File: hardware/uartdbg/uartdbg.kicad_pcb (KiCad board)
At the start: 2 copper layers, 40 x 16.5 mm, 20 parts, among them IC1 LM1117MP-3.3, J1 USB_B_Mini, J2 Conn_01x05_Female, J3 Conn_01x06_Female, U1 CH340N

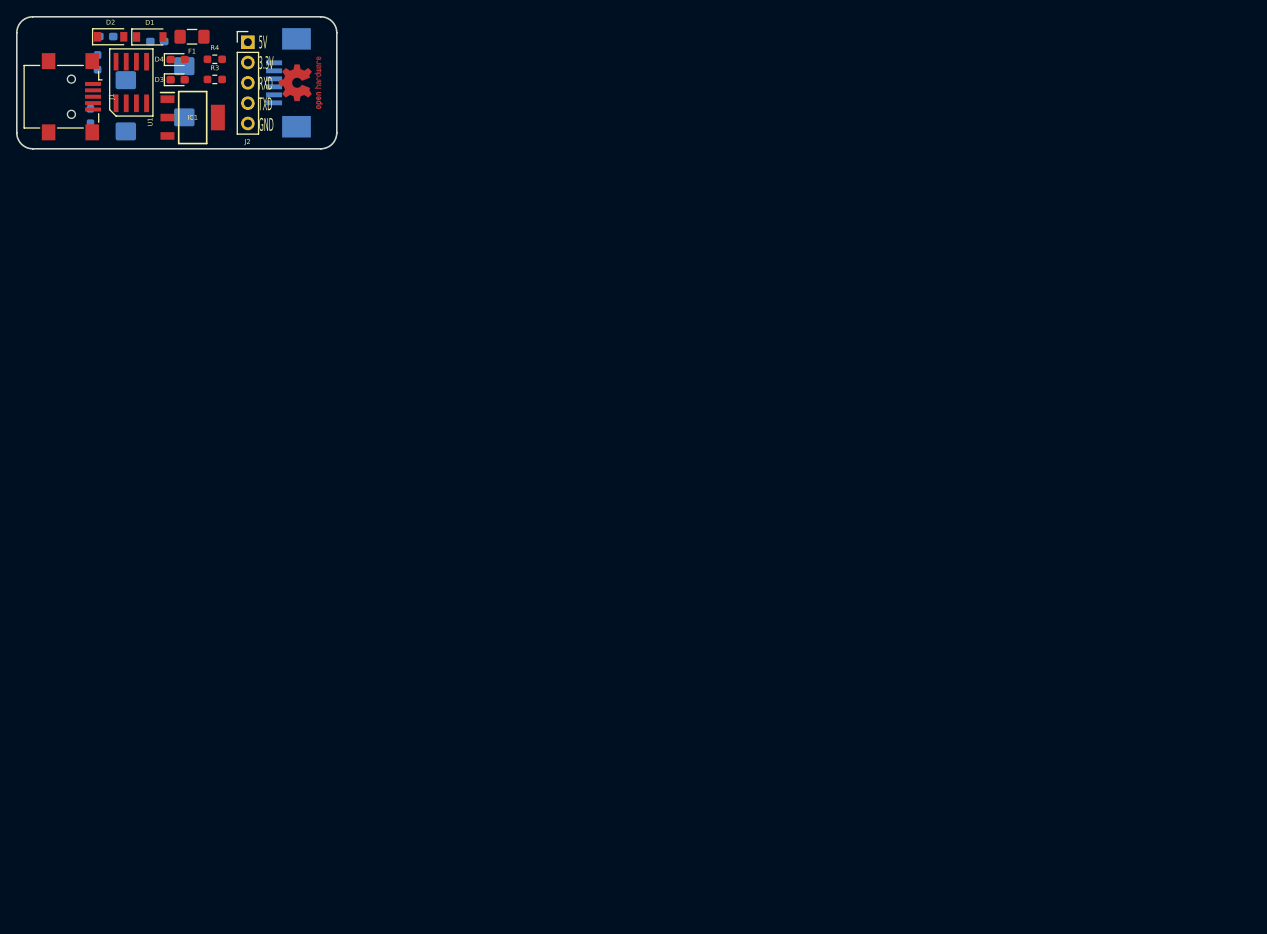
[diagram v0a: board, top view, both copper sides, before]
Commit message: [CHG][ADD][NT] 更新原理图和 PCB,添加额外的保护以及 logo,添加 geber 文件包
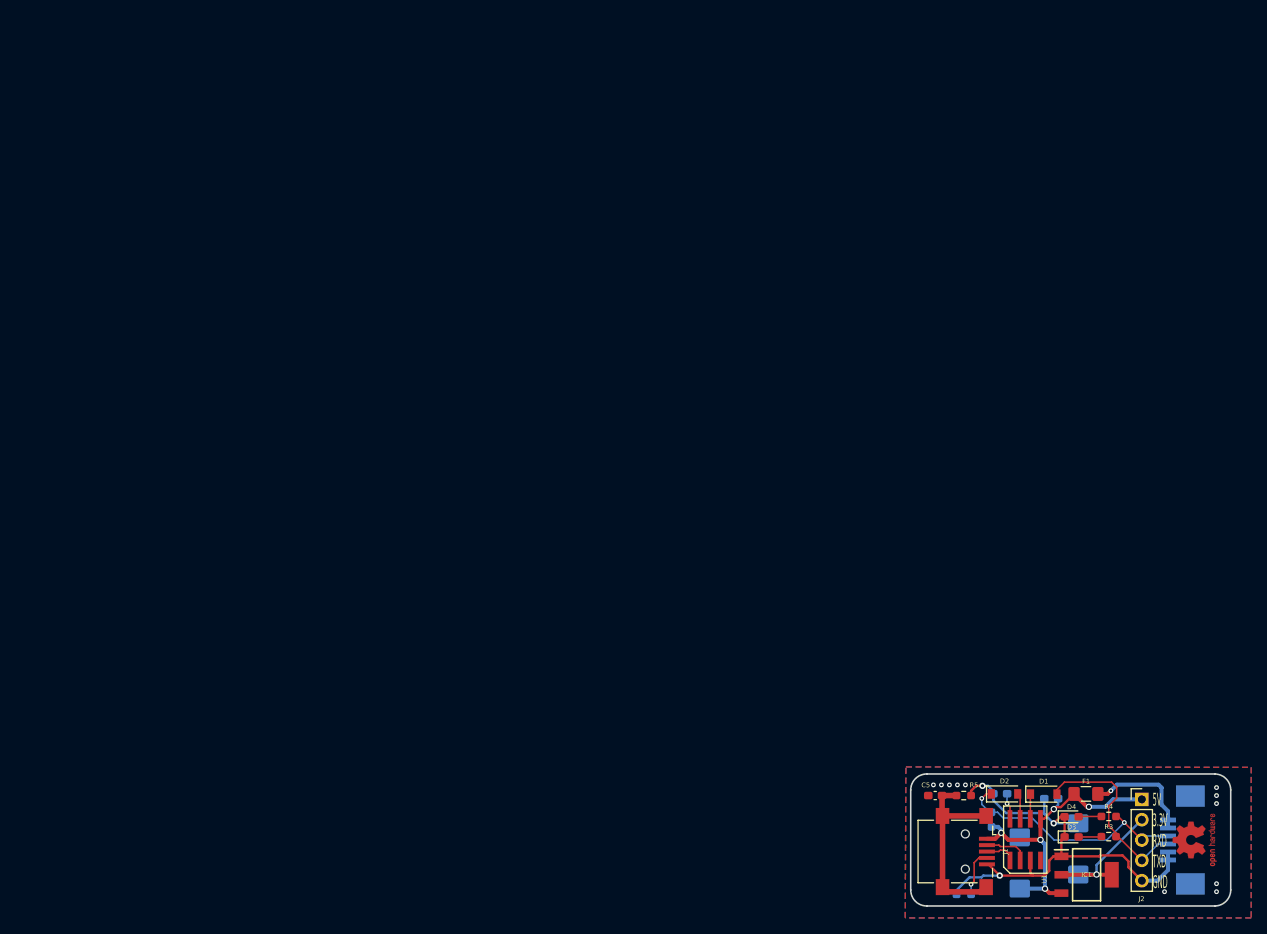
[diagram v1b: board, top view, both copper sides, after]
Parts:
- removed REF**: OSHW-Logo2_7.3x6mm_Copper, Symbol:OSHW-Logo2_7.3x6mm_Copper
- added C5: 4.7nf, Red_Pro:C_0603_1608Metric_Pad1.08x0.95mm_HandSolder, F.Cu at (112.8, 80.8)
- added LOGO1: Logo_Open_Hardware_Small, Symbol:OSHW-Logo2_7.3x6mm_Copper, F.Cu at (145.2, 86.4)
- added R5: 1M, Red_Pro:R_0603_1608Metric_Pad0.98x0.95mm_HandSolder, F.Cu at (116.4, 80.8)
- D3, D4: footprint LED_SMD:LED_0603_1608Metric_Pad1.05x0.95mm_HandSolder -> Red_Pro:LED_0603_1608Metric_Pad1.05x0.95mm_HandSolder
- moved REF_1 146.7 mm to (113.4, 86.2)
- moved C1 146.4 mm to (123.4, 89.3)
- moved C2 146.4 mm to (120.9, 80.6)
- moved D2 146.4 mm to (121.5, 80.6)
- moved F1 146.4 mm to (131.6, 80.6)
- moved IC1 146.4 mm to (131.7, 90.7)
- moved J3 146.4 mm to (143.7, 86.4)
- moved U1 146.4 mm to (124.1, 86.4)
- moved C3 146.4 mm to (130.7, 87.5)
- moved C4 146.4 mm to (127.3, 81.2), turned to 0 degrees
- moved D1 146.4 mm to (126.4, 80.7)
- moved D3 146.4 mm to (129.8, 86.0)
- moved D4 146.4 mm to (129.8, 83.5)
- moved J2 146.4 mm to (138.6, 81.3)
- moved R2 146.4 mm to (119.8, 83.8)
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- renumbered REF** to REF_1
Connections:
- J1 pad 6: GND -> Net-(C5-Pad1)
- R1 pad 1: Net-(J1-Pad4) -> GND
- R1 pad 2: GND -> Net-(J1-Pad4)
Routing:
- net GND: track 0.00 -> 64.1 mm, vias 0 -> 11
- net +5V: track 0.00 -> 40.3 mm, vias 0 -> 5
- net /TTL_RX: track 0.00 -> 30.7 mm, vias 0 -> 2
- net Net-(C5-Pad1): track 0.00 -> 25.3 mm
- net /TTL_TX: track 0.00 -> 24.2 mm
- net +3V3: track 0.00 -> 17.8 mm, vias 0 -> 1
- net /FUSE_5V: track 0.00 -> 14.0 mm, vias 0 -> 1
- net Net-(J1-Pad4): track 0.00 -> 5.97 mm, vias 0 -> 1
- net /USB_N: track 0.00 -> 5.65 mm
- net /USB_P: track 0.00 -> 3.86 mm
- net Net-(C2-Pad2): track 0.00 -> 3.30 mm, vias 0 -> 1
- net Net-(D2-Pad2): track 0.00 -> 3.24 mm
- net Net-(D1-Pad1): track 0.00 -> 3.10 mm
- net Net-(D4-Pad2): track 0.00 -> 2.87 mm
- net Net-(D3-Pad2): track 0.00 -> 2.87 mm
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- added copper zone on B.Cu, net GND
- added copper zone on F.Cu, net GND
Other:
- net class power5v added: clearance 0.2, trace_width 0.5, via_dia 0.8, via_drill 0.5

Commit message: [CHG][NT] 更新原理图和 PCB 对 TX 和 RX LED 灯具状态指示管脚接线为上拉
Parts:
- R3, R4: value 4.7k -> 510
- turned D3 to 180 degrees
- turned D4 to 180 degrees
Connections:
- D3 pad 1: GND -> Net-(D3-Pad1)
- D3 pad 2: Net-(D3-Pad2) -> +5V
- D4 pad 1: GND -> Net-(D4-Pad1)
- D4 pad 2: Net-(D4-Pad2) -> +5V
- R3 pad 1: Net-(D3-Pad2) -> Net-(D3-Pad1)
- R4 pad 1: Net-(D4-Pad2) -> Net-(D4-Pad1)
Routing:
- net GND: track 64.1 -> 57.3 mm
- net +5V: track 40.3 -> 44.5 mm
- net Net-(D4-Pad2): track 2.87 -> 0.00 mm
- net Net-(D4-Pad1): track 0.00 -> 2.87 mm
- net Net-(D3-Pad2): track 2.87 -> 0.00 mm
- net Net-(D3-Pad1): track 0.00 -> 2.87 mm
